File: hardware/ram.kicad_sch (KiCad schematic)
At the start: 15 parts, among them U10 IS42S16320D-6BLI, U4 GateMate-CCGM1A1

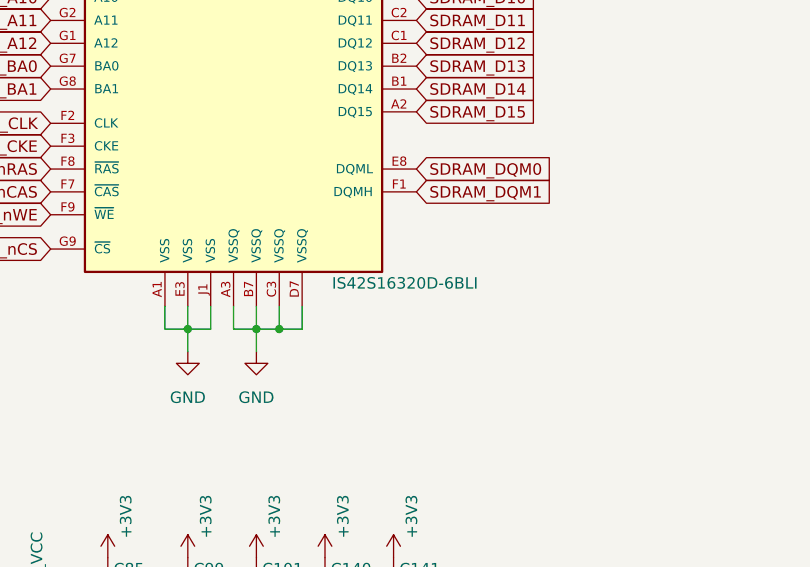
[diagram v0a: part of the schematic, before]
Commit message: Improve SerDes routing, tunning ETH pairs, moving parts - fix #31
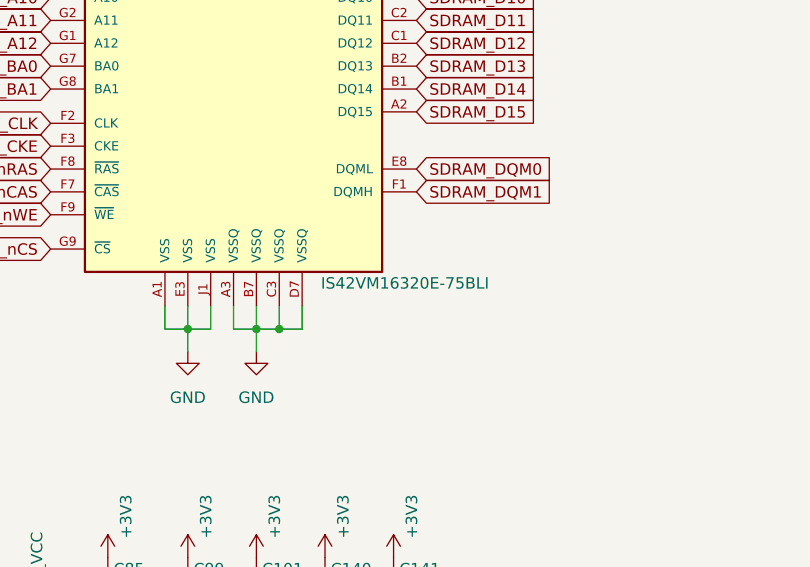
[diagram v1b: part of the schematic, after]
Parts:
- C101, C140, C141, C99: LCSC (none) -> C5340014; MPN CX0603MRX7R8BB223 -> GRM155R60J223KA01D; Mouser (none) -> https://www.mouser.in/ProductDetail/Pulse-Electronics/CX060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; Mouser Part Number (none) -> 81-GRM155R60J223KA1D
- C57, C76, C79, C80: LCSC (none) -> C1525; MPN (none) -> GRM155R60J104KA01D; Mouser (none) -> https://hr.mouser.com/ProductDetail/Murata-Electronics/GRM1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; Mouser Part Number (none) -> 81-GRM155R60J104KA1D
- C58, C77: LCSC (none) -> C15525; MPN (none) -> CL05A226MQ5N6J8; Mouser (none) -> https://hr.mouser.com/ProductDetail/Samsung-Electro-Mechani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; Mouser Part Number (none) -> 187-CL05A226MQ5N6J8
- C75, C78, C85: LCSC (none) -> C12530; MPN (none) -> CL05A225MQ5NSNC; Mouser (none) -> https://hr.mouser.com/ProductDetail/Samsung-Electro-Mechani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; Mouser Part Number (none) -> 187-CL05A225MQ5NSNC
- U10: value IS42S16320D-6BLI -> IS42VM16320E-75BLI; MPN (none) -> IS42VM16320E-75BLI; Mouser (none) -> https://hr.mouser.com/ProductDetail/ISSI/IS42VM16320E-75BLI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; Mouser Part Number (none) -> 870-I42VM16320E75BLI
- U4: LCSC (none) -> CCGM1A1-BGA324; MPN (none) -> CCGM1A1-BGA324

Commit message: v0.5 update
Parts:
- C101, C140, C141, C99: Mouser https://www.mouser.in/ProductDetail/Pulse-Electronics/CX060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 -> https://eu.mouser.com/en/ProductDetail/Murata-Electronics/G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
- C58, C77: LCSC C15525 -> C7423886
- U10: LCSC (none) -> C1352683
